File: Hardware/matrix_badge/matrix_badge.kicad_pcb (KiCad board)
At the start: 2 copper layers, 30.5 x 40.6 mm, 40 parts, among them J1 Conn_02x03_Odd_Even, U1 ATTINY85-20SU

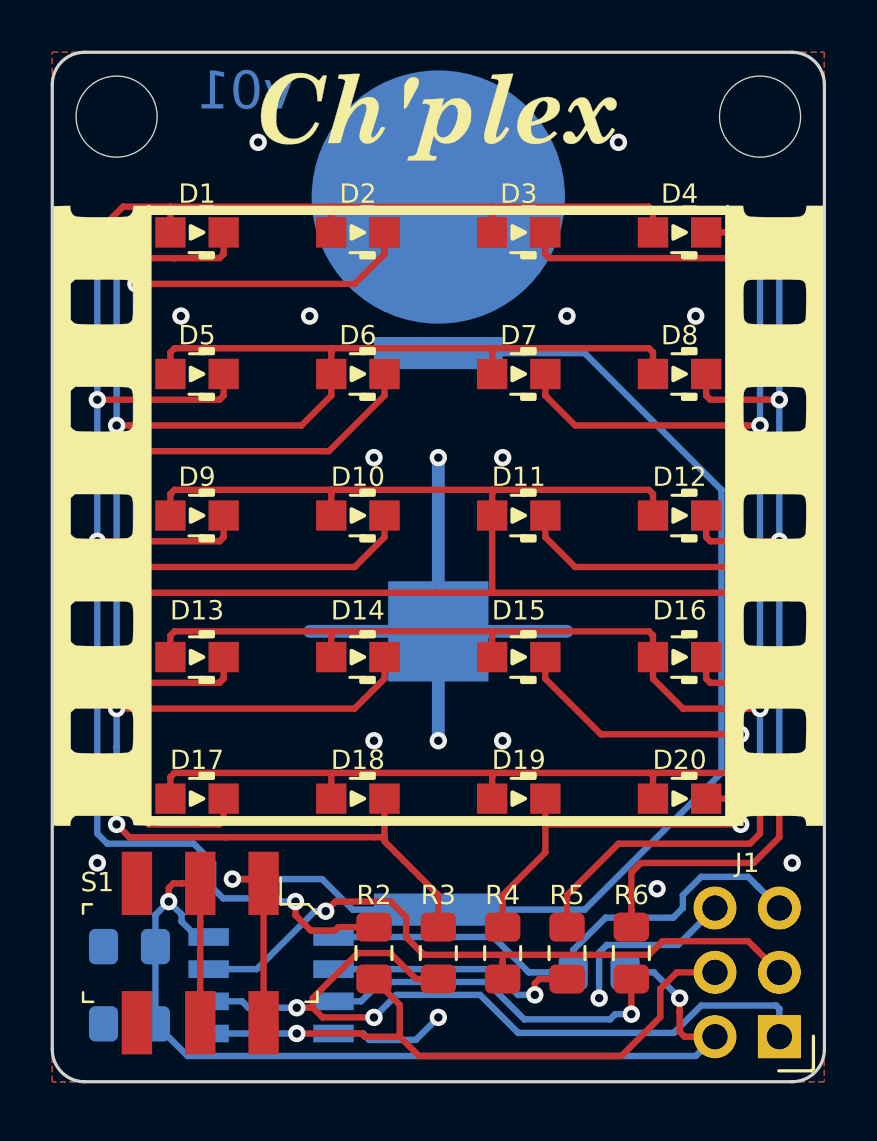
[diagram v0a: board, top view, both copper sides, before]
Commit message: Made fixes for v02 (added wide body SOIC and swapped round pin for rectangular pin back). Added ON/OFF silk for v03.
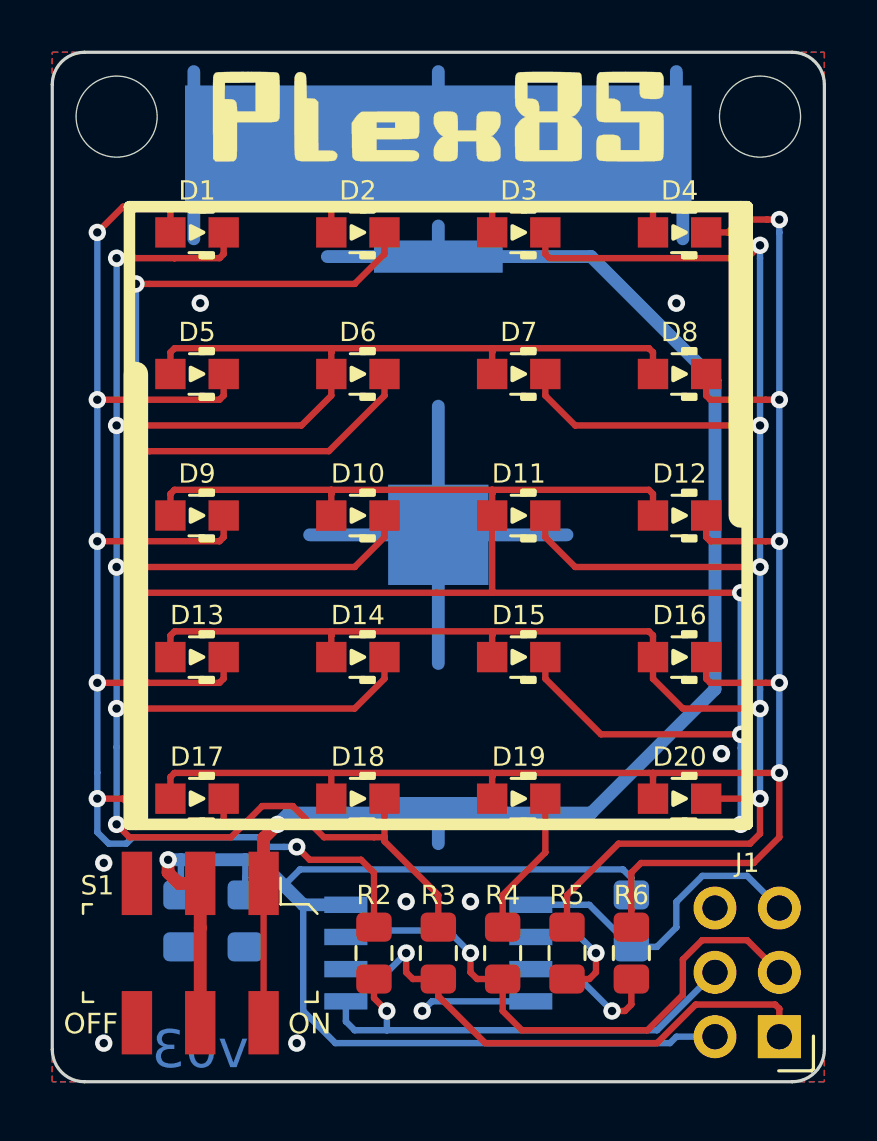
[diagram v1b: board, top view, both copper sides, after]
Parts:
- removed the G*** at (142.2, 78.7)
- removed the G*** at (142.2, 94.5)
- removed the REF** at (142.2, 81.9)
- added G***: LOGO, matrix_badge:plex85_logo, F.Cu at (142.2, 78.7)
- added PIN: pin_safety_sq_20mm, matrix_badge:pin_safety_sq_20mm, B.Cu at (142.2, 80.0)
- U1: footprint digikey-footprints:SOIC-8_W5.3mm -> Package_SO:SOIJ-8_5.3x5.3mm_P1.27mm
- moved REF** 29.9 mm to (153.7, 104.9)
- moved U1 6.73 mm to (142.2, 111.8)
- moved C2 4.68 mm to (134.6, 110.5), turned to 270 degrees
- moved C1 4.54 mm to (132.1, 110.5), turned to 270 degrees
- moved BT1 3.81 mm to (142.2, 95.2)
- moved G*** 3.68 mm to (153.7, 85.6)
- moved G*** 3.67 mm to (153.7, 87.5)
- moved R1 2.40 mm to (149.9, 110.5), turned to 270 degrees
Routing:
- net (no net): track 0.00 -> 53.8 mm
- net VDD: track 43.1 -> 53.9 mm, vias 2 -> 1
- net MISO: track 32.6 -> 22.2 mm, vias 2 -> 1
- net Net-(R6-Pad2): track 14.2 -> 5.77 mm
- net ~RST: track 21.1 -> 12.8 mm
- net GND: track 32.7 -> 24.8 mm, vias 17 -> 11
- net MOSI: track 25.1 -> 18.7 mm
- net Net-(BT1-Pad1): track 53.5 -> 59.8 mm
- net Net-(R5-Pad2): track 10.2 -> 4.85 mm
- net SCK: track 26.7 -> 22.9 mm
- net P2: track 100.8 -> 101.8 mm
- net P4: track 92.3 -> 93.0 mm
- net P5: track 74.8 -> 75.5 mm
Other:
- board text added: "/RST"
- board text added: "3V3"
- board text added: "Build Instructions:"
- board text added: "GND"
- board text added: "MISO"
- board text added: "MOSI"
- board text added: "OFF"
- board text added: "ON"
- board text added: "SCK"
- board text added: "bit.ly/plex85pcb"
- board text added: "v03"
- board text removed: "Instructions:"
- board text removed: "bit.ly/2WtfLSu"
- board text removed: "v01"
